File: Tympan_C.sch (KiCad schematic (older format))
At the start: 78 parts, among them J1 SJ-3523-SMT-TR, J2 SJ-3524-SMT-TR-PI, P10 CONN_02X01, P11 CONN_02X01, P2 CONN_01X04, P4 CONN_01X24, P5 CONN_01X01, P6 CONN_01X24, P7 CONN_02X01, P8 CONN_02X01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

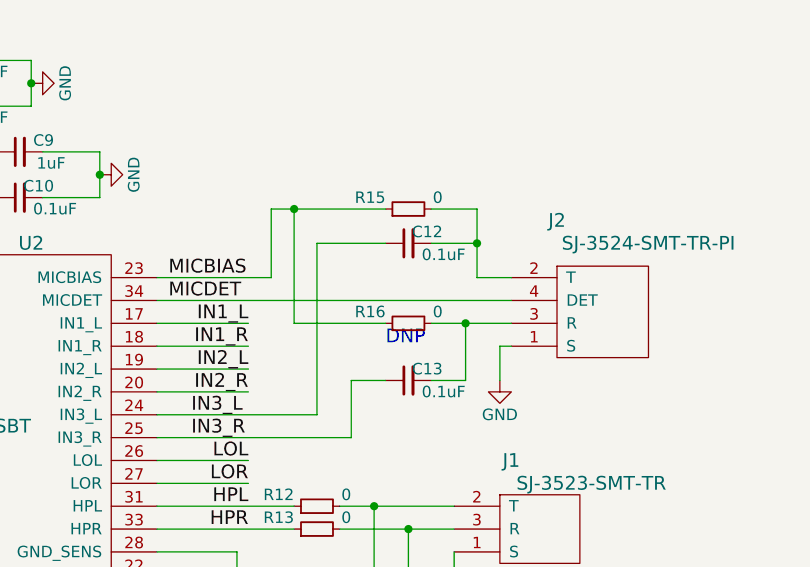
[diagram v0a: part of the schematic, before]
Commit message: Updated schematic
changed R15 to 2.2K
changed R16 to DNP
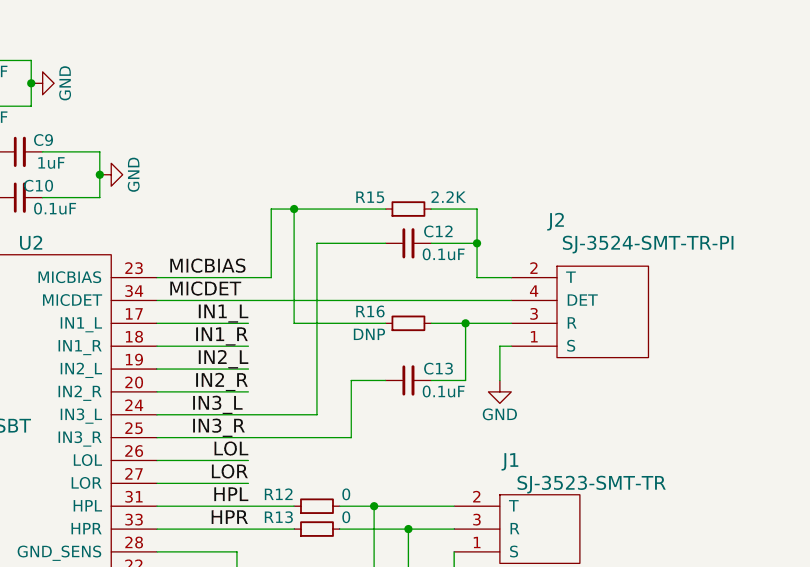
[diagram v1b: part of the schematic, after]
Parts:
- R15: value 0 -> 2.2K
- R16: value 0 -> DNP
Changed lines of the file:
@@
 LIBS:contrib
 LIBS:valves
-LIBS:OpenBCI
-LIBS:Solutions
 LIBS:Tympan
 LIBS:Tympan_C-cache
@@
 Sheet 1 1
 Title "Tympan Rev C"
-Date "6/1/2017"
+Date "8/21/2017"
 Rev "C"
 Comp "www.tympan.org"
@@
 P 7700 6700
 F 0 "R15" V 7750 6800 50  0000 L CNN
-F 1 "0" V 7750 6550 50  0000 L CNN
+F 1 "2.2K" V 7750 6450 50  0000 L CNN
 F 2 "Capacitors_SMD:C_0603" H 7700 6700 50  0001 C CNN
 F 3 "" H 7700 6700 50  0000 C CNN
@@
 P 7700 7200
 F 0 "R16" V 7750 7300 50  0000 L CNN
-F 1 "0" V 7750 7050 50  0000 L CNN
+F 1 "DNP" V 7650 7300 50  0000 L CNN
 F 2 "Capacitors_SMD:C_0603" H 7700 7200 50  0001 C CNN
 F 3 "" H 7700 7200 50  0000 C CNN
@@
 U 1 1 592F431A
 P 7700 6850
-F 0 "C12" V 7750 6700 50  0000 L CNN
+F 0 "C12" V 7750 6650 50  0000 L CNN
 F 1 "0.1uF" V 7650 6600 50  0000 L CNN
 F 2 "Capacitors_SMD:C_0402" H 7700 6850 50  0001 C CNN
@@
 U 1 1 592F456E
 P 7700 7450
-F 0 "C13" V 7750 7300 50  0000 L CNN
+F 0 "C13" V 7750 7250 50  0000 L CNN
 F 1 "0.1uF" V 7650 7200 50  0000 L CNN
 F 2 "Capacitors_SMD:C_0402" H 7700 7450 50  0001 C CNN
@@
 Text Notes 2800 8150 0    60   ~ 0
 DNP
-Text Notes 7600 7300 0    60   ~ 0
-DNP
-$Comp
+$Comp
